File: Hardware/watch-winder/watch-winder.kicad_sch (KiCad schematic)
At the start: 1 part, among them U1 STM32F030K6Tx

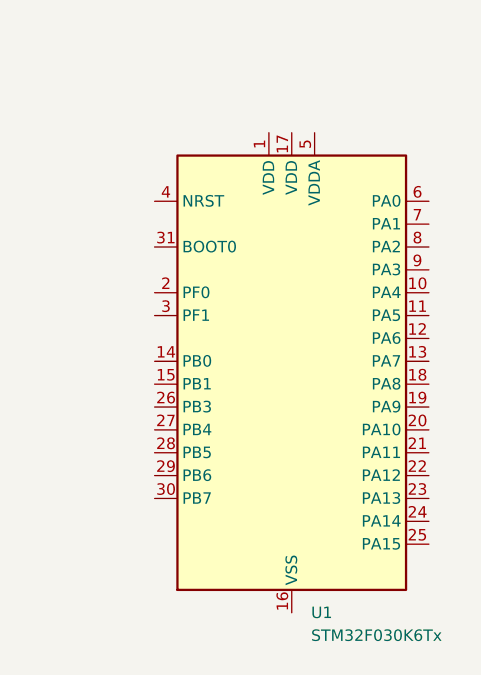
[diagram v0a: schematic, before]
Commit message: add decoupling caps
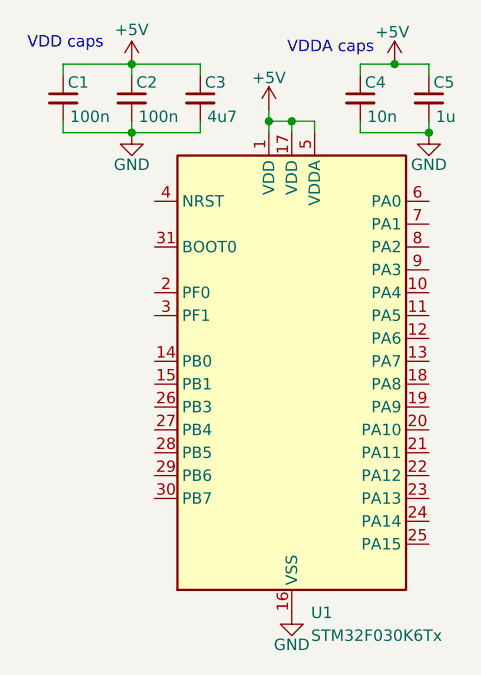
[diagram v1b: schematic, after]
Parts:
- added C1, C2: 100n, Capacitor_SMD:C_0805_2012Metric_Pad1.18x1.45mm_HandSolder, symbol Device:C_Small
- added C3: 4u7, Capacitor_SMD:C_0805_2012Metric_Pad1.18x1.45mm_HandSolder, symbol Device:C_Small
- added C4: 10n, Capacitor_SMD:C_0805_2012Metric_Pad1.18x1.45mm_HandSolder, symbol Device:C_Small
- added C5: 1u, Capacitor_SMD:C_0805_2012Metric_Pad1.18x1.45mm_HandSolder, symbol Device:C_Small
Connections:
- net +5V: now reaches U1.1 (VDD)
- net +5V: now also U1.17 (VDD), U1.5 (VDDA), C1.1, C2.1, C3.1, C4.1, C5.1
- net GND: now reaches U1.16 (VSS), U1.32 (VSS)
- net GND: now also C1.2, C2.2, C3.2, C4.2, C5.2
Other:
- note added: "VDD caps"
- note added: "VDDA caps"

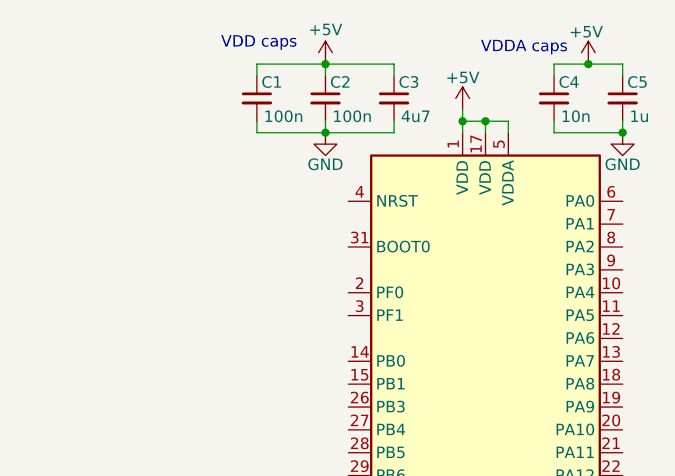
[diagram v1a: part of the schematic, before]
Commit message: add reset circuit, fix vdd
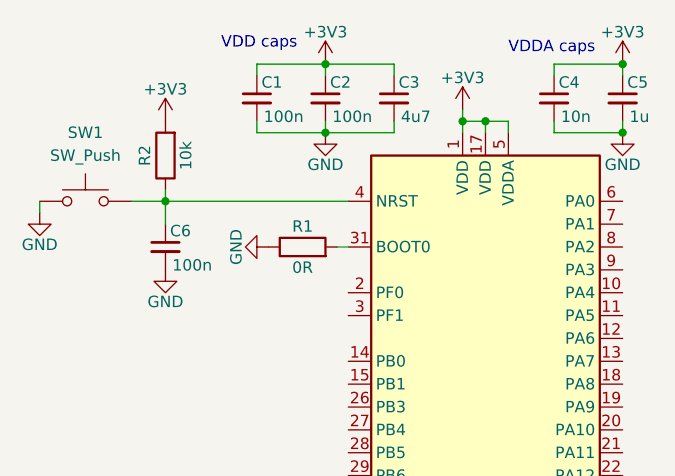
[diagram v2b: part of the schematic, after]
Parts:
- added C6: 100n, Capacitor_SMD:C_0805_2012Metric_Pad1.18x1.45mm_HandSolder, symbol Device:C_Small
- added R1: 0R, Resistor_SMD:R_0805_2012Metric_Pad1.20x1.40mm_HandSolder, symbol Device:R
- added R2: 10k, Resistor_SMD:R_0805_2012Metric_Pad1.20x1.40mm_HandSolder, symbol Device:R
- added SW1: SW_Push, Button_Switch_THT:SW_PUSH_6mm, symbol Switch:SW_Push
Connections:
- net GND: now also C6.2, R1.1, SW1.1
- net at U1.31 (BOOT0): now also R1.2
- net at U1.4 (NRST): now also C6.1, R2.1, SW1.2
- net +5V renamed +3V3
- net +3V3: now also R2.2

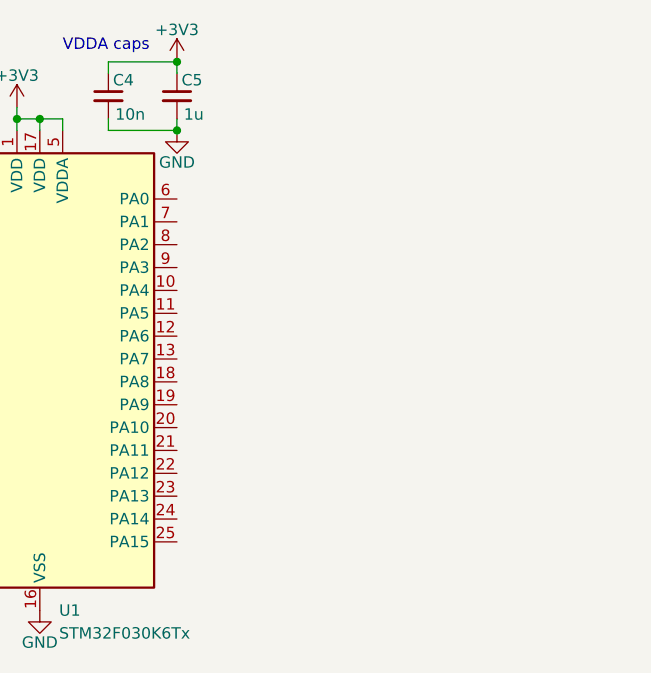
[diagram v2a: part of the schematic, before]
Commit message: add swd interface
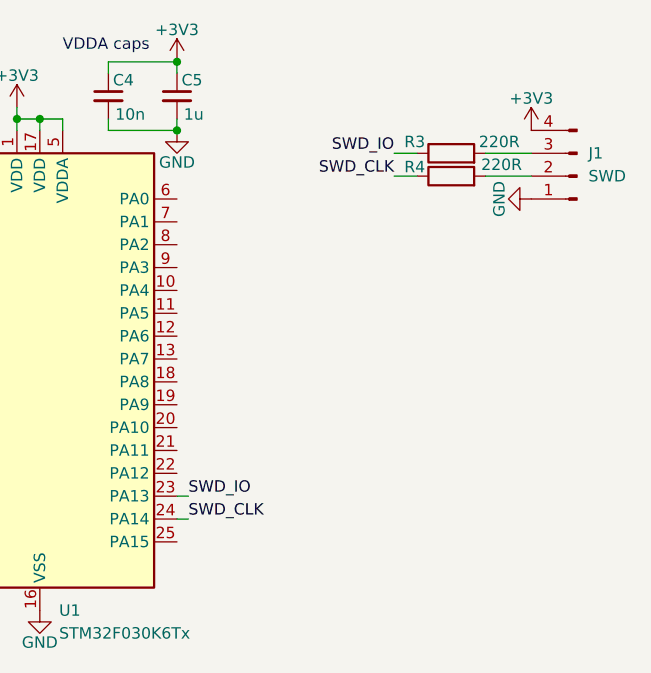
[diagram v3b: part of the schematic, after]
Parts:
- added J1: SWD, Connector_PinHeader_2.54mm:PinHeader_1x04_P2.54mm_Horizontal, symbol Connector:Conn_01x04_Pin
- added R3, R4: 220R, Resistor_SMD:R_0805_2012Metric_Pad1.20x1.40mm_HandSolder, symbol Device:R
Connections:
- net +3V3: now also J1.4 (Pin_4)
- net GND: now also J1.1 (Pin_1)
- net SWD_IO: now reaches U1.23 (PA13)
- net SWD_IO: now also R3.1
- net SWD_CLK: now reaches U1.24 (PA14)
- net SWD_CLK: now also R4.1
- new net: J1.2 (Pin_2), R4.2
- new net: J1.3 (Pin_3), R3.2

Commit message: add hse
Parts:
- added C7, C8: 20p, Capacitor_SMD:C_0805_2012Metric_Pad1.18x1.45mm_HandSolder, symbol Device:C_Small
- added Y1: 8M, Crystal:Crystal_HC49-U_Vertical, symbol Device:Crystal
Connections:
- net GND: now also C7.2, C8.2
- net at U1.2 (PF0): now also C7.1, Y1.2
- net at U1.3 (PF1): now also C8.1, Y1.1
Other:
- moved on the sheet: C6

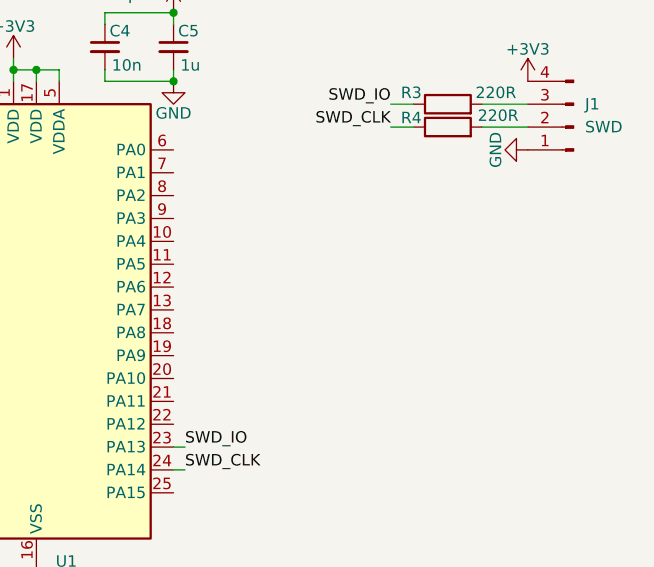
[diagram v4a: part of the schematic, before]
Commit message: add uart
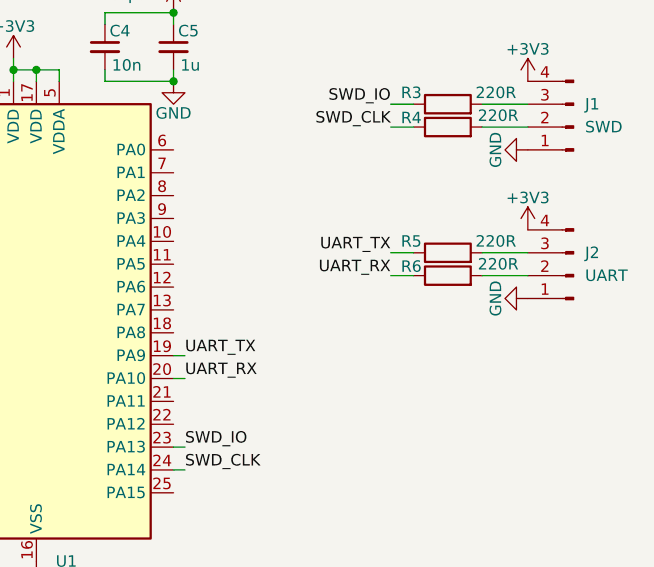
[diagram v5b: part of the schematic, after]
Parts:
- added J2: UART, Connector_PinHeader_2.54mm:PinHeader_1x04_P2.54mm_Horizontal, symbol Connector:Conn_01x04_Pin
- added R5, R6: 220R, Resistor_SMD:R_0805_2012Metric_Pad1.20x1.40mm_HandSolder, symbol Device:R
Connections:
- net +3V3: now also J2.4 (Pin_4)
- net GND: now also J2.1 (Pin_1)
- net UART_TX: now reaches U1.19 (PA9)
- net UART_TX: now also R5.1
- net UART_RX: now reaches U1.20 (PA10)
- net UART_RX: now also R6.1
- new net: J2.2 (Pin_2), R6.2
- new net: J2.3 (Pin_3), R5.2

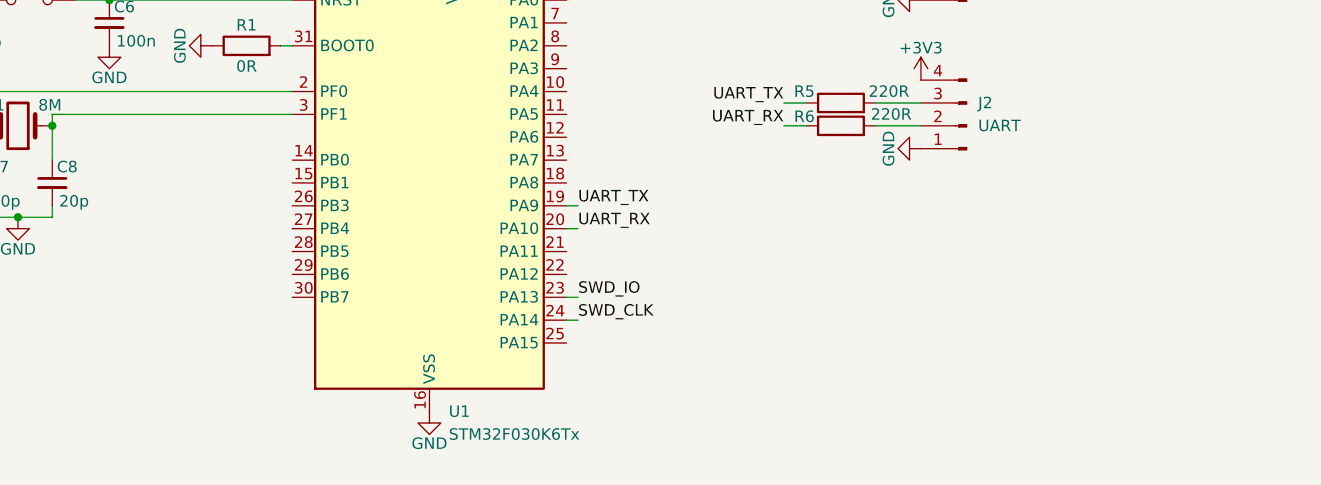
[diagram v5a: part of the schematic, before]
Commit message: add eeprom
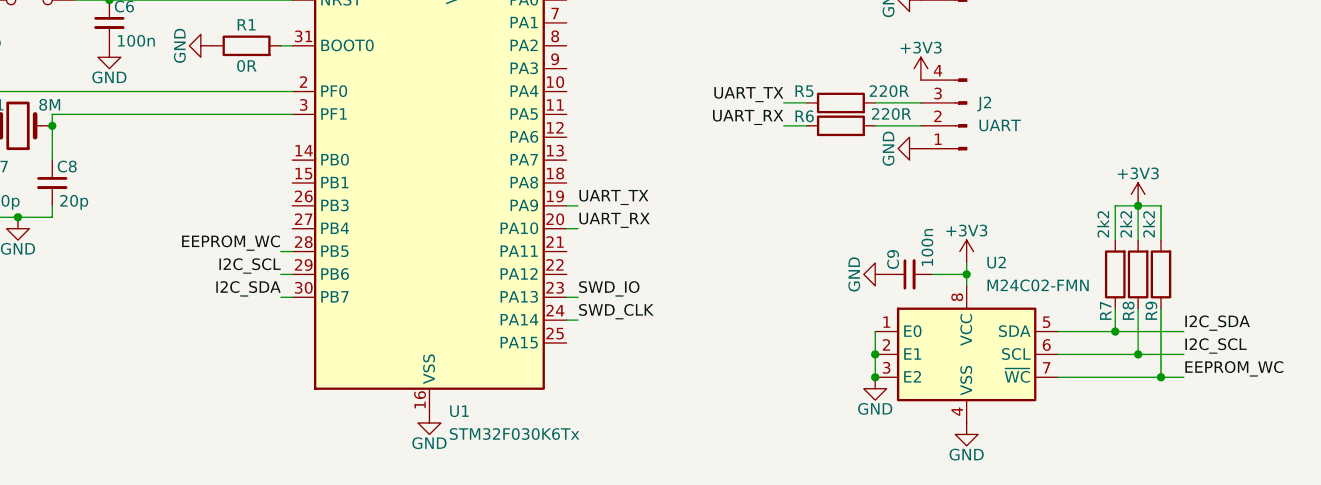
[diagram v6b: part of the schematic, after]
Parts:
- added C9: 100n, Capacitor_SMD:C_0805_2012Metric_Pad1.18x1.45mm_HandSolder, symbol Device:C_Small
- added R7, R8, R9: 2k2, Resistor_SMD:R_0805_2012Metric_Pad1.20x1.40mm_HandSolder, symbol Device:R
- added U2: M24C02-FMN, Package_SO:SOIC-8_3.9x4.9mm_P1.27mm, symbol Memory_EEPROM:M24C02-FMN
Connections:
- net +3V3: now also C9.2, R7.2, R8.2, R9.2, U2.8 (VCC)
- net GND: now also C9.1, U2.1 (E0), U2.2 (E1), U2.3 (E2), U2.4 (VSS)
- net EEPROM_WC: now reaches U1.28 (PB5)
- net EEPROM_WC: now also R9.1, U2.7 (~{WC})
- net I2C_SCL: now reaches U1.29 (PB6)
- net I2C_SCL: now also R8.1, U2.6 (SCL)
- net I2C_SDA: now reaches U1.30 (PB7)
- net I2C_SDA: now also R7.1, U2.5 (SDA)

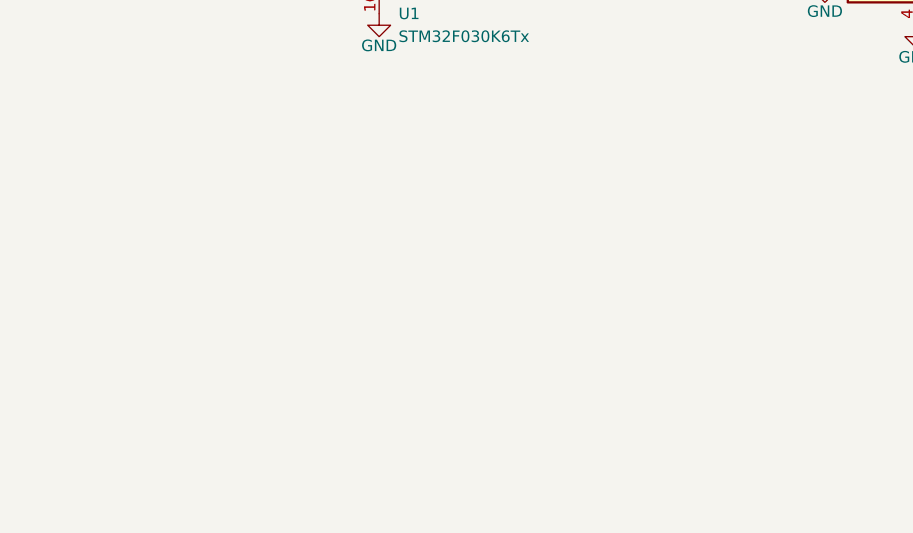
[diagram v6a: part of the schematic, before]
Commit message: add motor driver
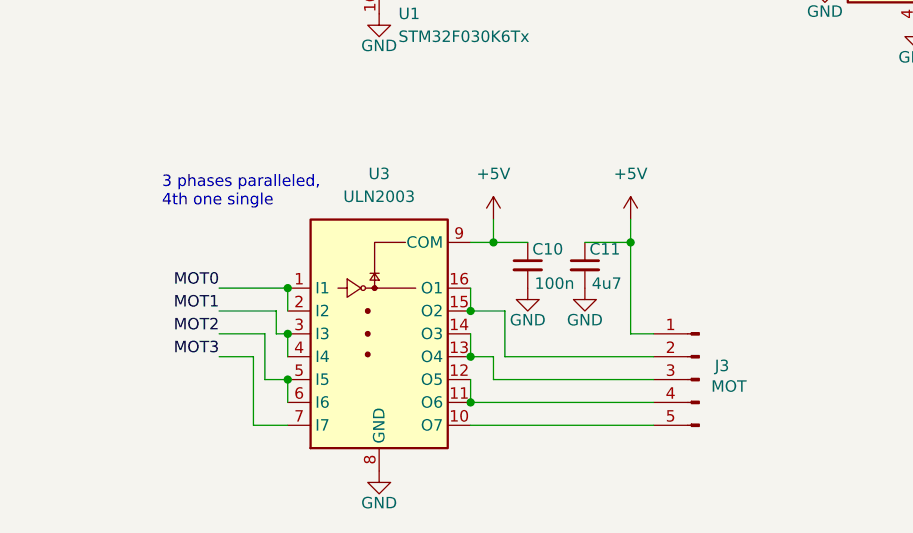
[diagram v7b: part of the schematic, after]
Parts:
- added C10: 100n, Capacitor_SMD:C_0805_2012Metric_Pad1.18x1.45mm_HandSolder, symbol Device:C_Small
- added C11: 4u7, Capacitor_SMD:C_0805_2012Metric_Pad1.18x1.45mm_HandSolder, symbol Device:C_Small
- added J3: MOT, Connector_PinHeader_2.54mm:PinHeader_1x05_P2.54mm_Vertical, symbol Connector:Conn_01x05_Pin
- added U3: ULN2003, Package_DIP:DIP-16_W7.62mm, symbol Transistor_Array:ULN2003
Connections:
- net GND: now also C10.2, C11.2, U3.8 (GND)
- new net: J3.2 (Pin_2), U3.15 (O2), U3.16 (O1)
- new net: J3.3 (Pin_3), U3.13 (O4), U3.14 (O3)
- new net: J3.4 (Pin_4), U3.11 (O6), U3.12 (O5)
- new net: J3.5 (Pin_5), U3.10 (O7)
- new net +5V: C10.1, C11.1, J3.1 (Pin_1), U3.9 (COM)
- new net MOT0: U3.1 (I1), U3.2 (I2)
- new net MOT1: U3.3 (I3), U3.4 (I4)
- new net MOT2: U3.5 (I5), U3.6 (I6)
- new net MOT3: U3.7 (I7)
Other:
- note added: "3 phases paralleled, 4th one single"

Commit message: add motor bus
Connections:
- net MOT0: now also U1.10 (PA4)
- net MOT1: now also U1.11 (PA5)
- net MOT2: now also U1.12 (PA6)
- net MOT3: now also U1.13 (PA7)
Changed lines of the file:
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@@
+	(wire
+		(pts
+			(xy 123.19 62.23) (xy 124.46 62.23)
+		)
+		(stroke
+			(width 0)
+			(type default)
+		)
+	)
 	(wire
 		(pts
@@
 	(wire
 		(pts
+			(xy 123.19 67.31) (xy 124.46 67.31)
+		)
+		(stroke
+			(width 0)
+			(type default)
+		)
+	)
+	(wire
+		(pts
 			(xy 189.23 91.44) (xy 191.77 91.44)
 		)
@@
 	(wire
 		(pts
+			(xy 123.19 59.69) (xy 124.46 59.69)
+		)
+		(stroke
+			(width 0)
+			(type default)
+		)
+	)
+	(wire
+		(pts
 			(xy 93.98 140.97) (xy 93.98 133.35)
 		)
@@
 		(pts
 			(xy 184.15 83.82) (xy 184.15 86.36)
+		)
+		(stroke
+			(width 0)
+			(type default)
+		)
+	)
+	(wire
+		(pts
+			(xy 123.19 64.77) (xy 124.46 64.77)
 		)
 		(stroke
@@
 		)
 	)
+	(label "MOT2"
+		(at 124.46 64.77 0)
+		(effects
+			(font
+				(size 1.27 1.27)
+			)
+			(justify left bottom)
+		)
+	)
 	(label "MOT0"
 		(at 90.17 125.73 180)
@@
 		)
 	)
+	(label "MOT3"
+		(at 124.46 67.31 0)
+		(effects
+			(font
+				(size 1.27 1.27)
+			)
+			(justify left bottom)
+		)
+	)
+	(label "MOT1"
+		(at 124.46 62.23 0)
+		(effects
+			(font
+				(size 1.27 1.27)
+			)
+			(justify left bottom)
+		)
+	)
 	(label "UART_TX"
 		(at 124.46 72.39 0)
@@
 		(effects
 			(font
+				(size 1.27 1.27)
+			)
+			(justify left bottom)
+		)
+	)
+	(label "MOT0"
+		(at 124.46 59.69 0)
+		(effects
+			(font
